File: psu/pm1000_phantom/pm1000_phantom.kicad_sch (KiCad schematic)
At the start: 17 parts, among them J1 Conn_01x03, J10 Conn_01x03, J2 48V in, J3 power led, J4 Conn_01x03, J5 Phantom A switch, J6 Phantom A led, J7 Conn_01x03, J8 Phantom B switch, J9 Phantom B led

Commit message: rename phantom board files and do some placement
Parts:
- J1: renamed from J2; footprint Connector_Molex:Molex_KK-396_A-41791-0002_1x02_P3.96mm_Vertical -> Connector_Molex:Molex_KK-254_AE-6410-02A_1x02_P2.54mm_Vertical
- J10: renamed from J3; footprint Connector_Molex:Molex_KK-396_A-41791-0002_1x02_P3.96mm_Vertical -> Connector_Molex:Molex_KK-254_AE-6410-02A_1x02_P2.54mm_Vertical
- J2: renamed from J5; footprint Connector_Molex:Molex_KK-396_A-41791-0002_1x02_P3.96mm_Vertical -> Connector_Molex:Molex_KK-254_AE-6410-02A_1x02_P2.54mm_Vertical
- J3: renamed from J8; footprint Connector_Molex:Molex_KK-396_A-41791-0002_1x02_P3.96mm_Vertical -> Connector_Molex:Molex_KK-254_AE-6410-02A_1x02_P2.54mm_Vertical
- J4: renamed from J6; footprint Connector_Molex:Molex_KK-396_A-41791-0002_1x02_P3.96mm_Vertical -> Connector_Molex:Molex_KK-254_AE-6410-02A_1x02_P2.54mm_Vertical
- J5: renamed from J9; footprint Connector_Molex:Molex_KK-396_A-41791-0002_1x02_P3.96mm_Vertical -> Connector_Molex:Molex_KK-254_AE-6410-02A_1x02_P2.54mm_Vertical
- J6: renamed from J1; value Conn_01x03 -> Chan A out; footprint Connector_Molex:Molex_KK-396_A-41791-0003_1x03_P3.96mm_Vertical -> Connector_Molex:Molex_KK-254_AE-6410-03A_1x03_P2.54mm_Vertical
- J7: renamed from J4; value Conn_01x03 -> Chan A int; footprint Connector_Molex:Molex_KK-396_A-41791-0003_1x03_P3.96mm_Vertical -> Connector_Molex:Molex_KK-254_AE-6410-03A_1x03_P2.54mm_Vertical
- J8: renamed from J7; value Conn_01x03 -> Chan B out; footprint Connector_Molex:Molex_KK-396_A-41791-0003_1x03_P3.96mm_Vertical -> Connector_Molex:Molex_KK-254_AE-6410-03A_1x03_P2.54mm_Vertical
- J9: renamed from J10; value Conn_01x03 -> Chan B int; footprint Connector_Molex:Molex_KK-396_A-41791-0003_1x03_P3.96mm_Vertical -> Connector_Molex:Molex_KK-254_AE-6410-03A_1x03_P2.54mm_Vertical
- renumbered R7 to R2, R9 to R5, R10 to R6, R2 to R7
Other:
- moved on the sheet: J1

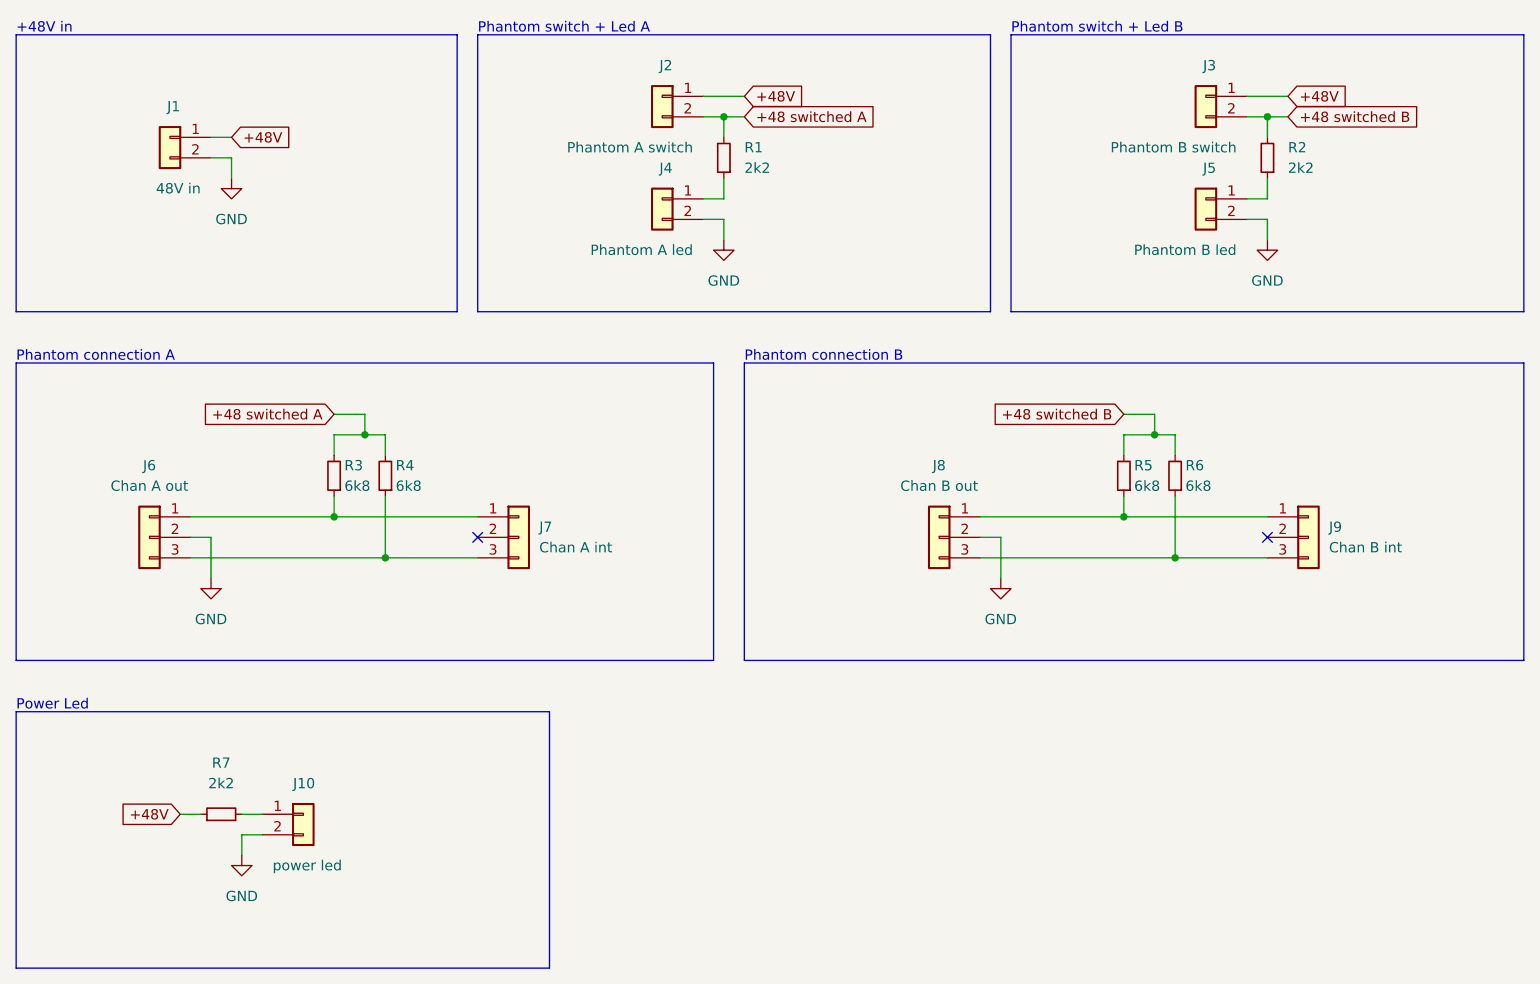
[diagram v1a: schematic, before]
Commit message: update phantom board
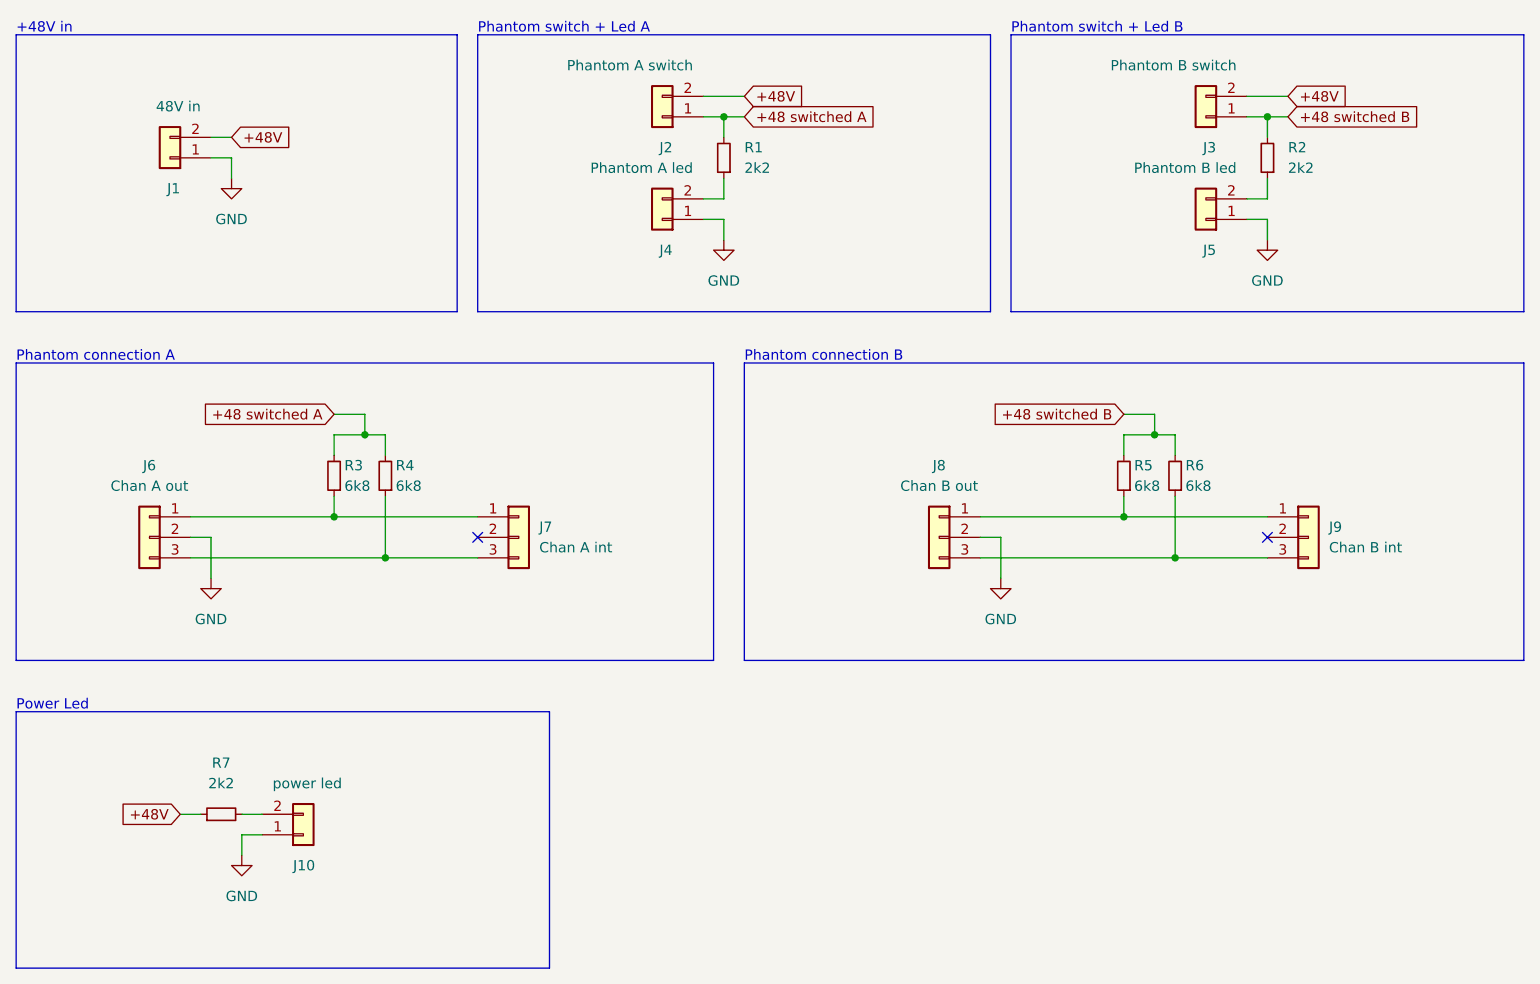
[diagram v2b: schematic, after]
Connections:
- net +48 switched A: now also J2.1 (Pin_1); no longer J2.2 (Pin_2)
- net +48 switched B: now also J3.1 (Pin_1); no longer J3.2 (Pin_2)
- net +48V: now also J1.2 (Pin_2), J2.2 (Pin_2), J3.2 (Pin_2); no longer J1.1 (Pin_1), J2.1 (Pin_1), J3.1 (Pin_1)
- net GND: now also J1.1 (Pin_1), J10.1 (Pin_1), J4.1 (Pin_1), J5.1 (Pin_1); no longer J1.2 (Pin_2), J10.2 (Pin_2), J4.2 (Pin_2), J5.2 (Pin_2)
- net at R1.1: now also J4.2 (Pin_2); no longer J4.1 (Pin_1)
- net at R7.2: now also J10.2 (Pin_2); no longer J10.1 (Pin_1)
- net at R2.1: now also J5.2 (Pin_2); no longer J5.1 (Pin_1)
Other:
- moved on the sheet: J1, J2, J3, J4, J5
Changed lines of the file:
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@@
     (pin "3")
   )
-  (symbol (lib_id "Connector_Generic:Conn_01x02") (at 99.06 39.37 0) (mirror y) (unit 1)
-    (in_bom yes) (on_board yes)
-    (property "Reference" "J4" (id 0) (at 100.33 35.56 0)
-      (effects (font (size 1.27 1.27)) (justify left))
-    )
-    (property "Value" "Phantom A led" (id 1) (at 102.87 45.72 0)
-      (effects (font (size 1.27 1.27)) (justify left))
-    )
-    (property "Footprint" "Connector_Molex:Molex_KK-254_AE-6410-02A_1x02_P2.54mm_Vertical" (id 2) (at 99.06 39.37 0)
-      (effects (font (size 1.27 1.27)) hide)
-    )
-    (property "Datasheet" "~" (id 3) (at 99.06 39.37 0)
+  (symbol (lib_id "Connector_Generic:Conn_01x02") (at 99.06 41.91 180) (unit 1)
+    (in_bom yes) (on_board yes)
+    (property "Reference" "J4" (id 0) (at 100.33 45.72 0)
+      (effects (font (size 1.27 1.27)) (justify left))
+    )
+    (property "Value" "Phantom A led" (id 1) (at 102.87 35.56 0)
+      (effects (font (size 1.27 1.27)) (justify left))
+    )
+    (property "Footprint" "Connector_Molex:Molex_KK-254_AE-6410-02A_1x02_P2.54mm_Vertical" (id 2) (at 99.06 41.91 0)
+      (effects (font (size 1.27 1.27)) hide)
+    )
+    (property "Datasheet" "~" (id 3) (at 99.06 41.91 0)
       (effects (font (size 1.27 1.27)) hide)
     )
@@
     (pin "1")
   )
-  (symbol (lib_id "Connector_Generic:Conn_01x02") (at 54.61 115.57 0) (unit 1)
-    (in_bom yes) (on_board yes)
-    (property "Reference" "J10" (id 0) (at 53.34 111.76 0)
-      (effects (font (size 1.27 1.27)) (justify left))
-    )
-    (property "Value" "power led" (id 1) (at 50.8 121.92 0)
-      (effects (font (size 1.27 1.27)) (justify left))
-    )
-    (property "Footprint" "Connector_Molex:Molex_KK-254_AE-6410-02A_1x02_P2.54mm_Vertical" (id 2) (at 54.61 115.57 0)
-      (effects (font (size 1.27 1.27)) hide)
-    )
-    (property "Datasheet" "~" (id 3) (at 54.61 115.57 0)
-      (effects (font (size 1.27 1.27)) hide)
-    )
-    (pin "1")
-    (pin "2")
-  )
-  (symbol (lib_id "Connector_Generic:Conn_01x02") (at 99.06 26.67 0) (mirror y) (unit 1)
-    (in_bom yes) (on_board yes)
-    (property "Reference" "J2" (id 0) (at 100.33 22.86 0)
-      (effects (font (size 1.27 1.27)) (justify left))
-    )
-    (property "Value" "Phantom A switch" (id 1) (at 102.87 33.02 0)
-      (effects (font (size 1.27 1.27)) (justify left))
-    )
-    (property "Footprint" "Connector_Molex:Molex_KK-254_AE-6410-02A_1x02_P2.54mm_Vertical" (id 2) (at 99.06 26.67 0)
-      (effects (font (size 1.27 1.27)) hide)
-    )
-    (property "Datasheet" "~" (id 3) (at 99.06 26.67 0)
-      (effects (font (size 1.27 1.27)) hide)
-    )
-    (pin "1")
-    (pin "2")
-  )
-  (symbol (lib_id "Connector_Generic:Conn_01x02") (at 38.1 31.75 0) (mirror y) (unit 1)
-    (in_bom yes) (on_board yes)
-    (property "Reference" "J1" (id 0) (at 39.37 27.94 0)
-      (effects (font (size 1.27 1.27)) (justify left))
-    )
-    (property "Value" "48V in" (id 1) (at 41.91 38.1 0)
-      (effects (font (size 1.27 1.27)) (justify left))
-    )
-    (property "Footprint" "Connector_Molex:Molex_KK-254_AE-6410-02A_1x02_P2.54mm_Vertical" (id 2) (at 38.1 31.75 0)
-      (effects (font (size 1.27 1.27)) hide)
-    )
-    (property "Datasheet" "~" (id 3) (at 38.1 31.75 0)
+  (symbol (lib_id "Connector_Generic:Conn_01x02") (at 54.61 118.11 0) (mirror x) (unit 1)
+    (in_bom yes) (on_board yes)
+    (property "Reference" "J10" (id 0) (at 53.34 121.92 0)
+      (effects (font (size 1.27 1.27)) (justify left))
+    )
+    (property "Value" "power led" (id 1) (at 50.8 111.76 0)
+      (effects (font (size 1.27 1.27)) (justify left))
+    )
+    (property "Footprint" "Connector_Molex:Molex_KK-254_AE-6410-02A_1x02_P2.54mm_Vertical" (id 2) (at 54.61 118.11 0)
+      (effects (font (size 1.27 1.27)) hide)
+    )
+    (property "Datasheet" "~" (id 3) (at 54.61 118.11 0)
+      (effects (font (size 1.27 1.27)) hide)
+    )
+    (pin "1")
+    (pin "2")
+  )
+  (symbol (lib_id "Connector_Generic:Conn_01x02") (at 99.06 29.21 180) (unit 1)
+    (in_bom yes) (on_board yes)
+    (property "Reference" "J2" (id 0) (at 100.33 33.02 0)
+      (effects (font (size 1.27 1.27)) (justify left))
+    )
+    (property "Value" "Phantom A switch" (id 1) (at 102.87 22.86 0)
+      (effects (font (size 1.27 1.27)) (justify left))
+    )
+    (property "Footprint" "Connector_Molex:Molex_KK-254_AE-6410-02A_1x02_P2.54mm_Vertical" (id 2) (at 99.06 29.21 0)
+      (effects (font (size 1.27 1.27)) hide)
+    )
+    (property "Datasheet" "~" (id 3) (at 99.06 29.21 0)
+      (effects (font (size 1.27 1.27)) hide)
+    )
+    (pin "1")
+    (pin "2")
+  )
+  (symbol (lib_id "Connector_Generic:Conn_01x02") (at 38.1 34.29 180) (unit 1)
+    (in_bom yes) (on_board yes)
+    (property "Reference" "J1" (id 0) (at 39.37 38.1 0)
+      (effects (font (size 1.27 1.27)) (justify left))
+    )
+    (property "Value" "48V in" (id 1) (at 41.91 27.94 0)
+      (effects (font (size 1.27 1.27)) (justify left))
+    )
+    (property "Footprint" "Connector_Molex:Molex_KK-254_AE-6410-02A_1x02_P2.54mm_Vertical" (id 2) (at 38.1 34.29 0)
+      (effects (font (size 1.27 1.27)) hide)
+    )
+    (property "Datasheet" "~" (id 3) (at 38.1 34.29 0)
       (effects (font (size 1.27 1.27)) hide)
     )
@@
     (pin "2")
   )
-  (symbol (lib_id "Connector_Generic:Conn_01x02") (at 166.37 39.37 0) (mirror y) (unit 1)
-    (in_bom yes) (on_board yes)
-    (property "Reference" "J5" (id 0) (at 167.64 35.56 0)
-      (effects (font (size 1.27 1.27)) (justify left))
-    )
-    (property "Value" "Phantom B led" (id 1) (at 170.18 45.72 0)
-      (effects (font (size 1.27 1.27)) (justify left))
-    )
-    (property "Footprint" "Connector_Molex:Molex_KK-254_AE-6410-02A_1x02_P2.54mm_Vertical" (id 2) (at 166.37 39.37 0)
-      (effects (font (size 1.27 1.27)) hide)
-    )
-    (property "Datasheet" "~" (id 3) (at 166.37 39.37 0)
+  (symbol (lib_id "Connector_Generic:Conn_01x02") (at 166.37 41.91 180) (unit 1)
+    (in_bom yes) (on_board yes)
+    (property "Reference" "J5" (id 0) (at 167.64 45.72 0)
+      (effects (font (size 1.27 1.27)) (justify left))
+    )
+    (property "Value" "Phantom B led" (id 1) (at 170.18 35.56 0)
+      (effects (font (size 1.27 1.27)) (justify left))
+    )
+    (property "Footprint" "Connector_Molex:Molex_KK-254_AE-6410-02A_1x02_P2.54mm_Vertical" (id 2) (at 166.37 41.91 0)
+      (effects (font (size 1.27 1.27)) hide)
+    )
+    (property "Datasheet" "~" (id 3) (at 166.37 41.91 0)
       (effects (font (size 1.27 1.27)) hide)
     )
@@
     (pin "3")
   )
-  (symbol (lib_id "Connector_Generic:Conn_01x02") (at 166.37 26.67 0) (mirror y) (unit 1)
-    (in_bom yes) (on_board yes)
-    (property "Reference" "J3" (id 0) (at 167.64 22.86 0)
-      (effects (font (size 1.27 1.27)) (justify left))
-    )
-    (property "Value" "Phantom B switch" (id 1) (at 170.18 33.02 0)
-      (effects (font (size 1.27 1.27)) (justify left))
-    )
-    (property "Footprint" "Connector_Molex:Molex_KK-254_AE-6410-02A_1x02_P2.54mm_Vertical" (id 2) (at 166.37 26.67 0)
-      (effects (font (size 1.27 1.27)) hide)
-    )
-    (property "Datasheet" "~" (id 3) (at 166.37 26.67 0)
-      (effects (font (size 1.27 1.27)) hide)
-    )
+  (symbol (lib_id "Connector_Generic:Conn_01x02") (at 166.37 29.21 180) (unit 1)
+    (in_bom yes) (on_board yes)
+    (property "Reference" "J3" (id 0) (at 167.64 33.02 0)
+      (effects (font (size 1.27 1.27)) (justify left))
+    )
+    (property "Value" "Phantom B switch" (id 1) (at 170.18 22.86 0)
+      (effects (font (size 1.27 1.27)) (justify left))
+    )
+    (property "Footprint" "Connector_Molex:Molex_KK-254_AE-6410-02A_1x02_P2.54mm_Vertical" (id 2) (at 166.37 29.21 0)
+      (effects (font (size 1.27 1.27)) hide)
+    )
+    (property "Datasheet" "~" (id 3) (at 166.37 29.21 0)
+      (effects (font (size 1.27 1.27)) hide)
+    )

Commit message: update boms with (some) mouser part numbers add 100n capacitors add power leds add frontpanel power led connector to psu board
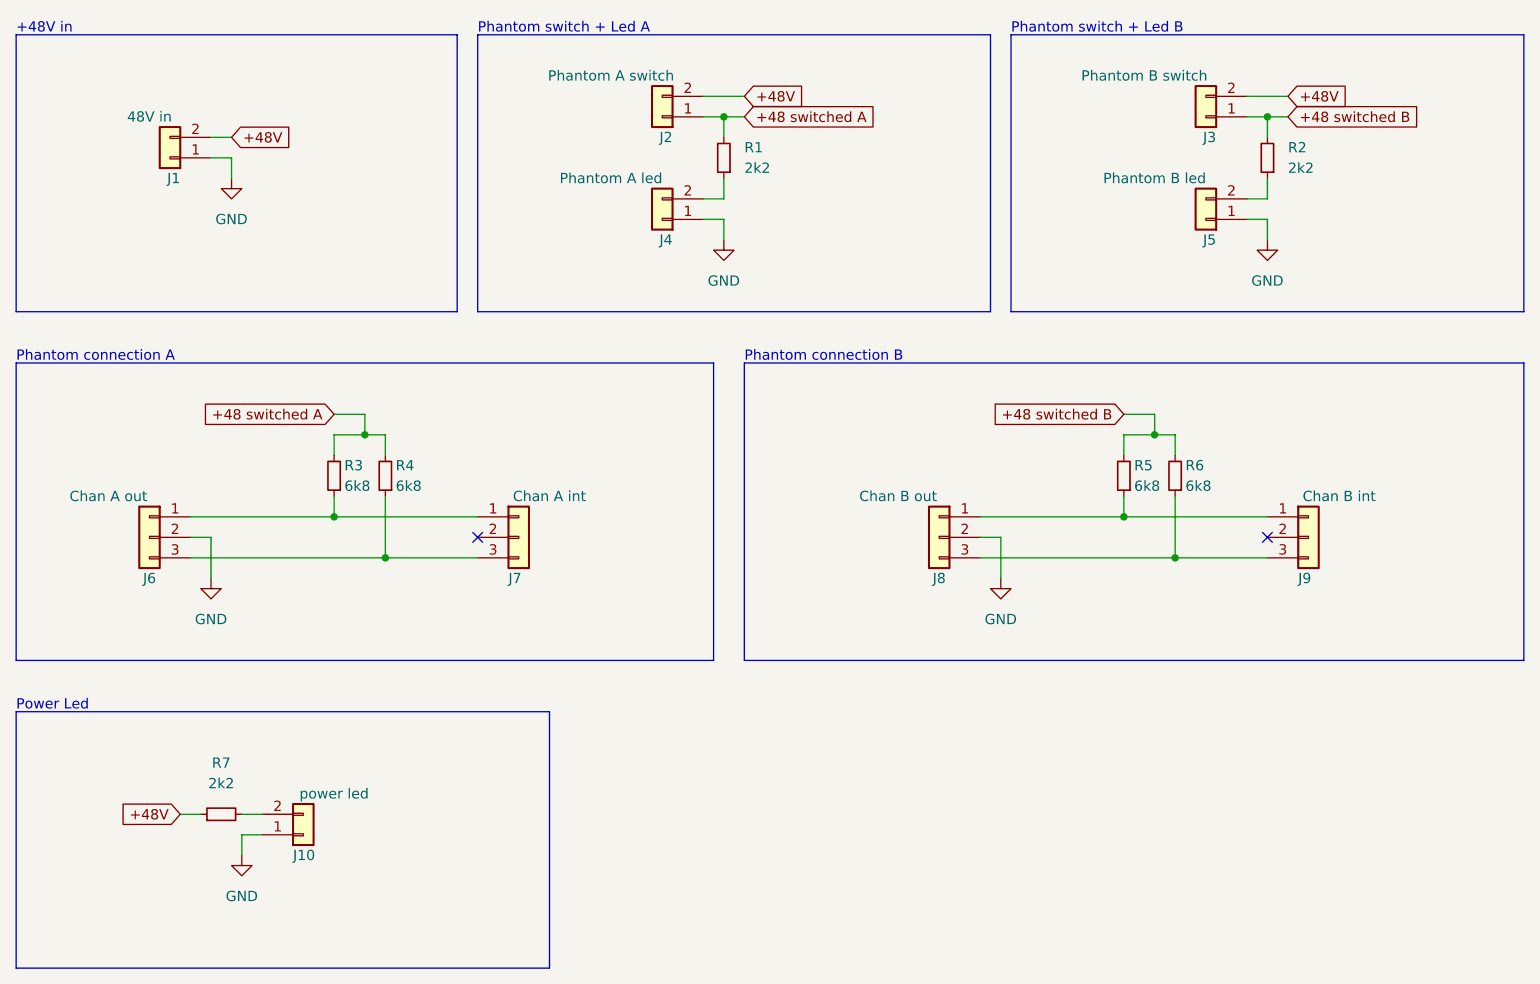
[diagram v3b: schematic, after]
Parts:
- J1: value 48V in -> 2 pin 2,54mm Molex; Function (none) -> 48V in; Mouser # (none) -> 538-22-23-2028
- J10: value power led -> 2 pin 2,54mm Molex; Function (none) -> power led; Mouser # (none) -> 538-22-23-2028
- J2: value Phantom A switch -> 2 pin 2,54mm Molex; Function (none) -> Phantom A switch; Mouser # (none) -> 538-22-23-2028
- J3: value Phantom B switch -> 2 pin 2,54mm Molex; Function (none) -> Phantom B switch; Mouser # (none) -> 538-22-23-2028
- J4: value Phantom A led -> 2 pin 2,54mm Molex; Function (none) -> Phantom A led; Mouser # (none) -> 538-22-23-2028
- J5: value Phantom B led -> 2 pin 2,54mm Molex; Function (none) -> Phantom B led; Mouser # (none) -> 538-22-23-2028
- J6: value Chan A out -> 3 pin 2,54mm Molex; Function (none) -> Chan A out; Mouser # (none) -> 538-22-04-5032
- J7: value Chan A int -> 3 pin 2,54mm Molex; Function (none) -> Chan A int; Mouser # (none) -> 538-22-04-5032
- J8: value Chan B out -> 3 pin 2,54mm Molex; Function (none) -> Chan B out; Mouser # (none) -> 538-22-04-5032
- J9: value Chan B int -> 3 pin 2,54mm Molex; Function (none) -> Chan B int; Mouser # (none) -> 538-22-04-5032
- R1, R2, R7: Mouser # (none) -> 603-MFR-25FRF52-2K2
- R3, R4, R5, R6: Mouser # (none) -> 603-MFR-25FRF52-6K8

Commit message: phantom board: connect mic input gnd
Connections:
- net GND: now also J7.2 (Pin_2), J9.2 (Pin_2)
- no-connect marks 2 -> 0
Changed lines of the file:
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@@
 (kicad_sch (version 20211123) (generator eeschema)
   (paper "A4")
+  (junction (at 43.18 81.28) (diameter 0) (color 0 0 0 0)
+  )
   (junction (at 156.21 78.74) (diameter 0) (color 0 0 0 0)
   )
@@
   (junction (at 62.23 68.58) (diameter 0) (color 0 0 0 0)
   )
+  (junction (at 140.97 81.28) (diameter 0) (color 0 0 0 0)
+  )
   (junction (at 160.02 68.58) (diameter 0) (color 0 0 0 0)
   )
-  (no_connect (at 76.2 81.28))
-  (no_connect (at 173.99 81.28))
   (polyline (pts (xy 139.7 53.34) (xy 76.2 53.34))
     (stroke (width 0) (type default) (color 0 0 0 0))
@@
     (stroke (width 0) (type default) (color 0 0 0 0))
   )
+  (wire (pts (xy 43.18 81.28) (xy 76.2 81.28))
+    (stroke (width 0) (type default) (color 0 0 0 0))
+  )
   (wire (pts (xy 156.21 71.12) (xy 156.21 68.58))
     (stroke (width 0) (type default) (color 0 0 0 0))
@@
     (stroke (width 0) (type default) (color 0 0 0 0))
   )
+  (wire (pts (xy 140.97 81.28) (xy 173.99 81.28))
+    (stroke (width 0) (type default) (color 0 0 0 0))
+  )

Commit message: set led resistors to 22k, place new psu terminal block
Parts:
- R1, R2, R7: value 2k2 -> 22k
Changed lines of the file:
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@@
 			)
 		)
-		(property "Value" "2k2"
+		(property "Value" "22k"
 			(at 44.45 111.76 90)
 			(effects
@@
 			)
 		)
-		(property "Value" "2k2"
+		(property "Value" "22k"
 			(at 176.53 35.5599 0)
 			(effects
@@
 			)
 		)
-		(property "Value" "2k2"
+		(property "Value" "22k"
 			(at 109.22 35.5599 0)
 			(effects
